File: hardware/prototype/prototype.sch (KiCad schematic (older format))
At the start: 17 parts

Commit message: semi-finaliseprototype gateway design
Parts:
- removed J?: Jack-DC, symbol Connector_Specialized:Jack-DC
- removed JP? (x6): SolderJumper_3_Open, symbol Jumper:SolderJumper_3_Open
- removed JP? (x3): SolderJumper_2_Open, symbol Jumper:SolderJumper_2_Open
- removed JP? (x2): SolderJumper_2_Bridged, symbol Jumper:SolderJumper_2_Bridged
- added C?: 10uF, symbol Device:C
- added C? (x4): 0.1uF, symbol Device:C
- added J?: Screw_Terminal_01x02, symbol Connector_Specialized:Screw_Terminal_01x02
- added J?: Conn_02x12_Odd_Even, symbol Connector_Generic:Conn_02x12_Odd_Even
- added J?: Battery-holder, symbol battery-holder:Battery-holder
- added J?: Conn_01x03, symbol Connector_Generic:Conn_01x03
- added J?: Conn_01x04, symbol Connector_Generic:Conn_01x04
- added JP? (x26): Jumper_NC_Dual, symbol Device:Jumper_NC_Dual
- added JP? (x2): Jumper_NC_Small, symbol Device:Jumper_NC_Small
- added JP? (x2): SolderJumper_2_Open, symbol Jumper:SolderJumper_2_Open
- added JP? (x3): Jumper_NO_Small, symbol Device:Jumper_NO_Small
- added R?: 10k, symbol Device:R
- added U?: LM2596_MODULE, symbol narra:LM2596_MODULE
- added U?: TLV71333PDBV, Package_TO_SOT_SMD:SOT-23-5, symbol Regulator_Linear:TLV71333PDBV
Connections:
- net labels added: (+)RAIL, (-)RAIL, 1, 10, 12, 14, 15, 16, 17, 18, 19, 2, 21, 22, 23, 24, 3V3_REF, 4, 5, 6, 7, 8, 9, CELLULAR_5V, CONTROLLER_RX, CONTROLLER_TX, CSN, GLOBAL_3V3, GLOBAL_5V, LoRa_5V, MISO, MOSI, PPS, RESET, SCK, TEMP_DATA, TEMP_SCK, V_BCKUP
- net labels removed: 5V, BRD_GPS_RST, HDR_GPS_RST
- wire segments 48 -> 192
- no-connect marks 13 -> 35
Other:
- note added: "3v power_management"
- note added: "5v Input voltage tie-point"
- note added: "5v power_management"
- note added: "Alternate_GPS"
- note added: "Alternative programming header"
- note added: "BAT-HLD-001-xx-OTL CR2032 battery holder"
- note added: "Backup current consumption 7uA @ 3v3(Quectel), 15uA Ublox"
- note added: "Backup supply selection for Cold or Warm/hotstart"
- note added: "Communication_module_header"
- note added: "DHT22 Temp, Humidity sensor\n(vertical)"
- note added: "LoRa concentrator connector(Top view), RF connector on left"
- note added: "On board GPS"
- note added: "RAK_concentrator"
- note added: "RHF0M301_concentrator"
- note added: "TODO\n1. Add reverse polarity protection.\n2. Add ESP32 connections\n3. Check the LAN/Cellular connection compatibility and complete communication header.\n4. Check 3D model availability and clashes\n5. Note items needed from digikey/mouser"
- note added: "UBLOX_GPS_header"
- note removed: "Alternative_GPS_header"
- note removed: "Kaiote standard LoRa concentrator connector"
- note removed: "Power_management"
- moved on the sheet: U?

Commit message: Add missing footprints
1. Think about lightning protection and use of GDTs and TVSs
2. Combine the various board and peripheral libraries into a single unified component.
3. The component should have mounting holes suitable for standoffs and cable ties.
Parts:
- removed C?: 0.1uF, symbol Device:C
- removed JP? (x2): Jumper_NC_Small, symbol Device:Jumper_NC_Small
- added C?: 1uF, symbol Device:C
- added C? (x3): 0.1uF, symbol Device:C
- added C? (x2): 10uF, symbol Device:CP
- added D?: LED, symbol Device:LED
- added MK? (x14): Mounting_Hole, symbol Mechanical:Mounting_Hole
- added Q?: DTC143Z, symbol Transistor_BJT:DTC143Z
- added Q?: Si2323, TO_SOT_Packages_SMD:SOT-23, symbol Si2323CDS:Si2323
- added R?: 200, symbol Device:R
- added TP?: Test_Point_Probe, symbol Connector_Specialized:Test_Point_Probe
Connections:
- net labels added: PPS_OUTPUT
- wire segments 192 -> 217
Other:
- note added: "3v3 power_management"
- note added: "Mounting hole for standoffs for GPS module"
- note added: "Mounting hole for standoffs for communication module"
- note added: "PCB mounting hole for controller module cable ties"
- note added: "PCB mounting holes for SMA connectors"
- note added: "PCB mounting holes for cellular module cable ties"
- note added: "PPS indicator"
- note removed: "3v power_management"
- note removed: "Communication_module_header"
- moved on the sheet: U?

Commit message: prototype gateway PCB creation checkpoint
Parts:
- removed C?: 10uF, symbol Device:C
- removed C?: 0.1uF, symbol Device:C
- removed J?: Conn_01x03, symbol Connector_Generic:Conn_01x03
- removed JP?: SolderJumper_2_Open, symbol Jumper:SolderJumper_2_Open
- removed JP? (x12): Jumper_NC_Dual, symbol Device:Jumper_NC_Dual
- removed JP? (x3): Jumper_NO_Small, symbol Device:Jumper_NO_Small
- removed MK? (x14): Mounting_Hole, symbol Mechanical:Mounting_Hole
- removed TP?: Test_Point_Probe, symbol Connector_Specialized:Test_Point_Probe
- removed U?: UBX_M8Q_GPS_HEADER, symbol quectel_L80:UBX_M8Q_GPS_HEADER
- added C10: 10uF, symbol Device:CP
- added C2, C9: 0.1uF, symbol Device:C
- added C3: 10uF, symbol Device:C
- added J1: 0734120114, digikey-footprints:Molex_734120114_UMC_RF_CONN_Vertical, symbol dk_Coaxial-Connectors-RF:0734120114
- added J4: Conn_01x04, symbol Connector_Generic:Conn_01x04
- added J5: Conn_02x07_Odd_Even, Connector_PinSocket_2.54mm:PinSocket_2x07_P2.54mm_Horizontal, symbol Connector_Generic:Conn_02x07_Odd_Even
- added JP17, JP18: Jumper, symbol Device:Jumper
- added JP19: SolderJumper_2_Open, symbol Jumper:SolderJumper_2_Open
- added JP6: Jumper_3_Open, Connector_PinHeader_2.54mm:PinHeader_1x03_P2.54mm_Vertical, symbol Jumper:Jumper_3_Open
- D1: renamed from D?; footprint (none) -> LED_SMD:LED_0805_2012Metric_Pad0.97x1.50mm_HandSolder
- J2: renamed from J?; footprint (none) -> Connector_PinSocket_2.54mm:PinSocket_1x04_P2.54mm_Vertical
- J6: renamed from J?; footprint (none) -> lib_fp:BAT-HLD-001-xx-OTL
- J7: renamed from J?; footprint (none) -> lib_fp:Hybrid_concentrator
- JP10, JP11, JP12, JP13, JP14, JP15, JP16, JP2, JP3, JP4, JP5, JP7, JP8, JP9: renamed from JP?; footprint (none) -> Connector_PinHeader_2.54mm:PinHeader_1x03_P2.54mm_Vertical
- Q1: renamed from Q?; purhase page (none) -> https://www.digikey.com/product-detail/en/on-semiconductor/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
- R1: renamed from R?; Population status (none) -> NC
- U1: renamed from U?; footprint (none) -> lib_fp:QUECTEL_L80-M39
- U4: renamed from U?; footprint (none) -> lib_fp:ESP32_DEVKITC
- gave numbers to parts that had none: 16
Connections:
- net labels added: 11, 20, 3, CLK, PPS_VISUAL, RMII-RX0, RMII_CLK, RMII_CRS_DV, RMII_MDC, RMII_MDIO, RMII_RX1, RMII_TX0, RMII_TX1, RMII_TX_EN
- net labels removed: 1, 10, 12, 18, 2, 24, 4, 7, 8, 9, BRD_GPS_VCC, GSM_CTS, GSM_RI, GSM_RTS, HDR_GPS_1PPS, HDR_GPS_RX, HDR_GPS_TX, HDR_GPS_VBCKUP, HDR_GPS_VCC, PPS, PPS_OUTPUT, TEMP_SCK
- wire segments 217 -> 225
- no-connect marks 35 -> 33
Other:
- note added: "Ethernet PHY connector(Waveshare LAN8720)"
- note added: "GPIO35-39 are input pins w/o internal pullup capability"
- note added: "GPS FIX indicator"
- note added: "Handle strapping pins GPIO 0 and GPIO 2 on boot"
- note added: "LoRa concentrator connector(Top view), SMA RF connector on left"
- note added: "Remove jumper on 5v rail when USB programming \nto avoid circulationg currents between supplies."
- note removed: "Alternate_GPS"
- note removed: "CTS_ENABLE(DISABLED DEFAULT)"
- note removed: "GPS select jumper"
- note removed: "LoRa concentrator connector(Top view), RF connector on left"
- note removed: "Mounting hole for standoffs for GPS module"
- note removed: "Mounting hole for standoffs for communication module"
- note removed: "On board GPS"
- note removed: "PCB mounting hole for controller module cable ties"
- note removed: "PCB mounting holes for SMA connectors"
- note removed: "PCB mounting holes for cellular module cable ties"
- note removed: "PPS indicator"
- note removed: "RI_ENABLE(DISABLED DEFAULT)"
- note removed: "RTS_ENABLE(DISABLED DEFAULT)"
- note removed: "UBLOX_GPS_header"
- moved on the sheet: C1, C6, C8, J7, JP11, JP15, JP7, JP9

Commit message: Complete schematic less mikroe ug95 footprint
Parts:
- removed J3: Screw_Terminal_01x02, symbol Connector_Specialized:Screw_Terminal_01x02
- added C13: 10uF, Capacitor_SMD:C_1206_3216Metric_Pad1.24x1.80mm_HandSolder, symbol Device:CP
- added C14, C15: 0.1uF, Capacitor_SMD:C_0805_2012Metric_Pad1.15x1.50mm_HandSolder, symbol Device:C
- added C16: 220uF, Capacitor_SMD:CP_Elec_6.3x5.8, symbol Device:CP
- added D2: LED, LED_SMD:LED_0805_2012Metric_Pad0.97x1.50mm_HandSolder, symbol Device:LED
- added J8: Jack-DC, Connector_BarrelJack:BarrelJack_Horizontal, symbol Connector_Specialized:Jack-DC
- added JP20: Jumper, Connector_PinSocket_2.54mm:PinSocket_1x02_P2.54mm_Vertical, symbol Device:Jumper
- added R3, R4, R7: 10k, Resistor_SMD:R_0805_2012Metric, symbol Device:R
- added R6: 270R, Resistor_SMD:R_0805_2012Metric, symbol Device:R
- added R8: 33R, Resistor_SMD:R_0805_2012Metric, symbol Device:R
- C1, C12, C2, C5, C8: footprint (none) -> Capacitor_SMD:C_0805_2012Metric_Pad1.15x1.50mm_HandSolder
- C10, C11: value 10uF -> 220uF; footprint (none) -> Capacitor_SMD:CP_Elec_6.3x5.8; purchase page (none) -> https://www.digikey.com/product-detail/en/nichicon/UUD0J221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
- C3: footprint (none) -> Capacitor_SMD:C_0805_2012Metric_Pad1.15x1.50mm_HandSolder; purchase page (none) -> https://www.digikey.com/product-detail/en/avx-corporation/T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
- C4: value 0.1uF -> 1uF; footprint (none) -> Capacitor_SMD:C_0805_2012Metric_Pad1.15x1.50mm_HandSolder; purchase page (none) -> https://www.digikey.com/product-detail/en/yageo/CC0805KKX7R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
- C6: footprint (none) -> Capacitor_SMD:C_1206_3216Metric_Pad1.24x1.80mm_HandSolder
- C7: value 1uF -> 0.1uF; footprint (none) -> Capacitor_SMD:C_0805_2012Metric_Pad1.15x1.50mm_HandSolder
- C9: value 0.1uF -> 100pF; footprint (none) -> Capacitor_SMD:C_0805_2012Metric_Pad1.15x1.50mm_HandSolder; purchase page (none) -> https://www.digikey.com/product-detail/en/avx-corporation/0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
- J4: footprint (none) -> Connector_PinHeader_2.54mm:PinHeader_1x04_P2.54mm_Vertical
- JP1, JP19: footprint (none) -> Jumper:SolderJumper-2_P1.3mm_Open_RoundedPad1.0x1.5mm
- JP17, JP18: footprint (none) -> Connector_PinSocket_2.54mm:PinSocket_1x02_P2.54mm_Vertical
- Q1: footprint (none) -> Package_TO_SOT_SMD:SC-59_Handsoldering; purchase page (none) -> https://www.digikey.com/product-detail/en/rohm-semiconducto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; purhase page https://www.digikey.com/product-detail/en/on-semiconductor/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 -> (none)
- Q2: purchase page (none) -> https://www.digikey.com/product-detail/en/vishay-siliconix/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
- R1, R2: footprint (none) -> Resistor_SMD:R_0805_2012Metric
- TP1: footprint (none) -> TestPoint:TestPoint_Pad_D1.0mm
- U2: purchase page (none) -> https://www.digikey.ca/product-detail/en/texas-instruments/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
- U3: footprint (none) -> lib_fp:LM2596_MODULE; purchase page (none) -> https://store.nerokas.co.ke/index.php?route=product/product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
- U4: purchase page (none) -> https://www.digikey.com/product-detail/en/espressif-systems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
- U5: purchase page (none) -> https://www.mikroe.com/3g-ea-click
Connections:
- net labels added: ESP32_5v, NETWORK_STATUS, PHY_POWER_EN, RMII_REFOSC_nINT
- net labels removed: (-)RAIL, 3V3, CLK, RMII_CLK
- wire segments 225 -> 271
- no-connect marks 33 -> 39
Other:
- note added: "1PPS output to LED/ uFL connector"
- note added: "Backup supply selection for SRAM in Cold or Warm/hotstart"
- note added: "Handle strapping pins GPIO 0, 2, 5, 12, 15 on boot\n(Set as outputs or handle their state on reset if inputs)"
- note added: "In RHF0M301 Datasheet p20, filtering \ncircuit on RESET line is ignored as \nthere are no mechanical components \non that line."
- note added: "LoRa concentrator connector(Top view), SMA RF connector on right"
- note added: "Network status LED\n=================\nToggles once every 500ms for a network error. Check network interfaces.\nToggles once every 30 sec for a successful uplink report."
- note added: "RMII_REFOSC_nINT should be a 33 ohm transmission line"
- note added: "Remove jumper on 5v rail when USB programming \nto avoid circulating currents between supplies."
- note removed: "Backup supply selection for Cold or Warm/hotstart"
- note removed: "Handle strapping pins GPIO 0 and GPIO 2 on boot"
- note removed: "LoRa concentrator connector(Top view), SMA RF connector on left"
- note removed: "Remove jumper on 5v rail when USB programming \nto avoid circulationg currents between supplies."
- note removed: "TODO\n1. Add reverse polarity protection.\n2. Add ESP32 connections\n3. Check the LAN/Cellular connection compatibility and complete communication header.\n4. Check 3D model availability and clashes\n5. Note items needed from digikey/mouser"
- moved on the sheet: C1, C10, C4, C8, J7, JP11, JP17

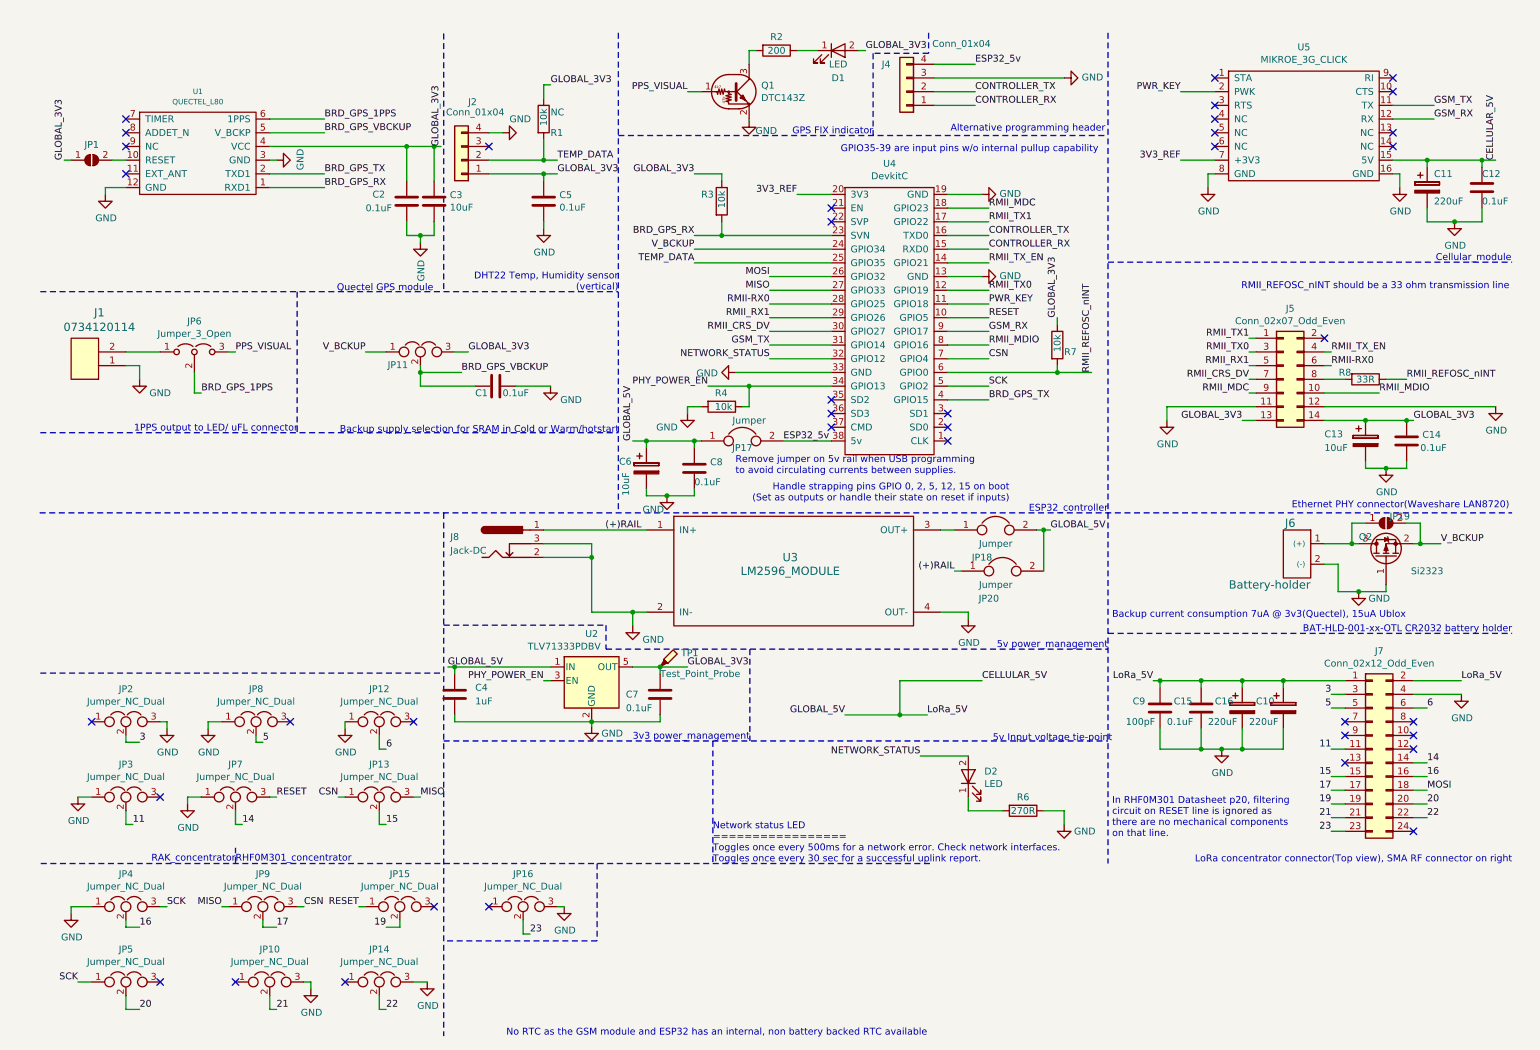
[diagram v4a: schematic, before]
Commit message: Complete schematic design less footprint asignment completion
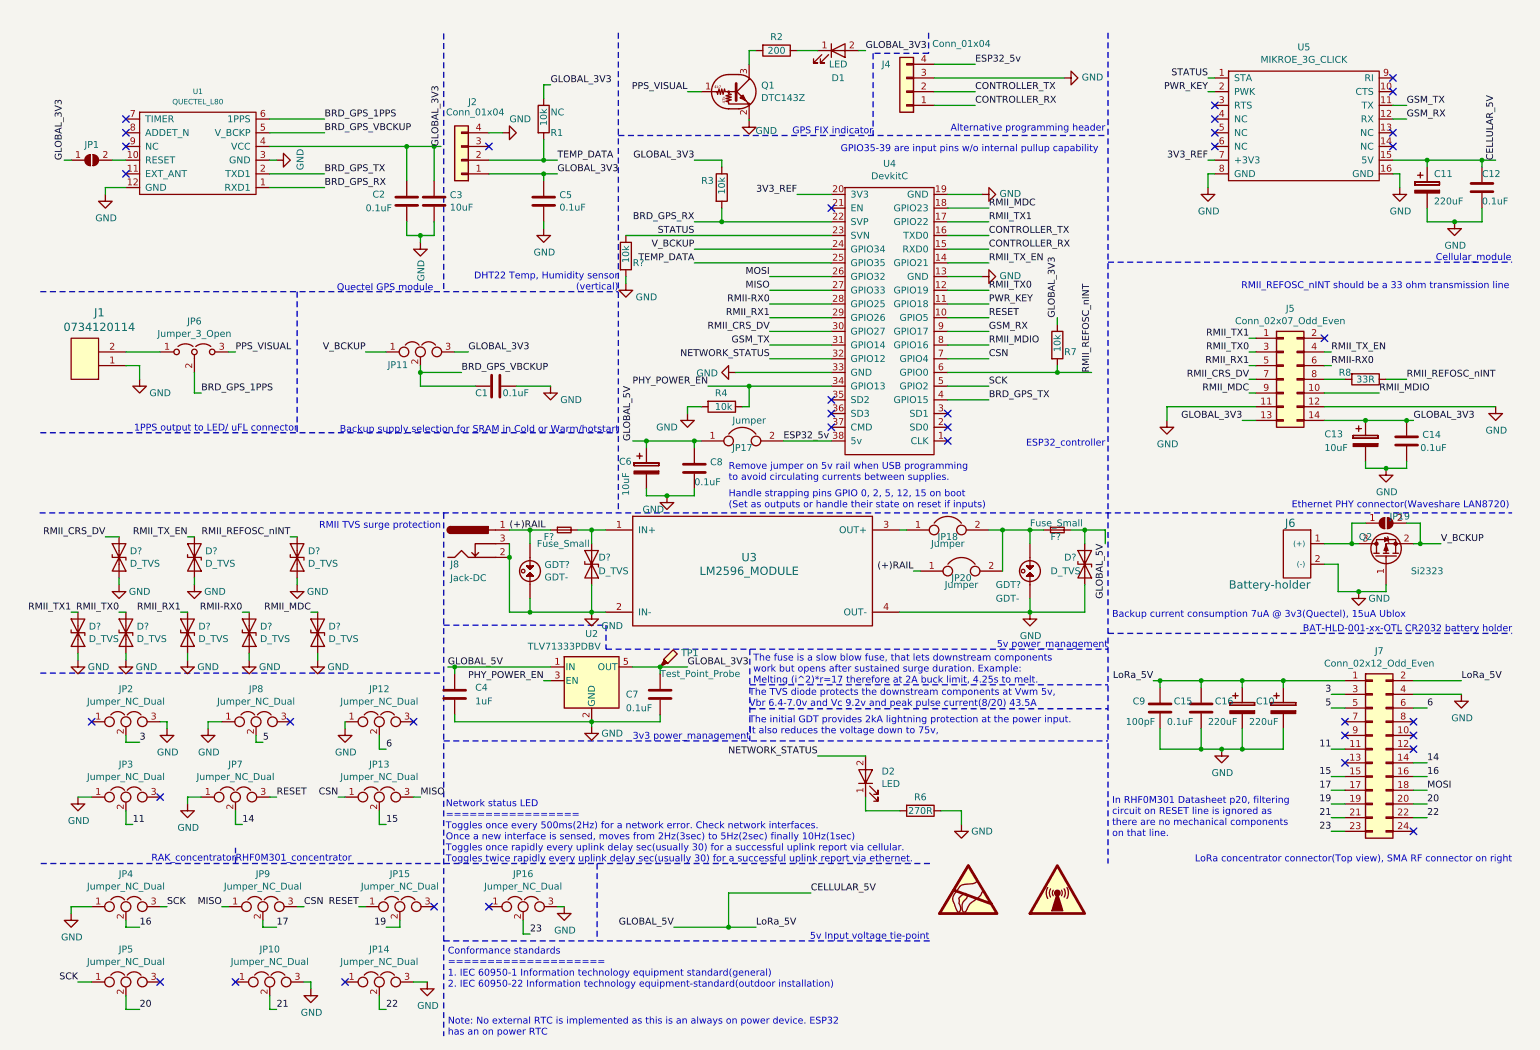
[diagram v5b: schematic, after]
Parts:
- added D? (x10): D_TVS, symbol Device:D_TVS
- added F? (x2): Fuse_Small, symbol Device:Fuse_Small
- added GDT? (x2): GDT-, symbol GDT-:GDT-
- added R?: 10k, symbol Device:R
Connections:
- net (+)RAIL: now also F?.1, GDT?.1; no longer U3.1 (IN+)
- net BRD_GPS_RX: now also U4.22 (SVP); no longer U4.23 (SVN)
- net CELLULAR_5V: now also D?.1 (A1), F?.2; no longer JP18.2, JP20.2
- net GND: now also D?.2 (A2), D?.2 (A2), D?.2 (A2), D?.2 (A2), D?.2 (A2), D?.2 (A2), D?.2 (A2), D?.2 (A2), D?.2 (A2), D?.2 (A2), GDT?.2, GDT?.2, R?.2
- net RMII-RX0: now also D?.1 (A1)
- net RMII_CRS_DV: now also D?.1 (A1)
- net RMII_MDC: now also D?.1 (A1)
- net RMII_REFOSC_nINT: now also D?.1 (A1)
- net RMII_RX1: now also D?.1 (A1)
- net RMII_TX0: now also D?.1 (A1)
- net RMII_TX1: now also D?.1 (A1)
- net RMII_TX_EN: now also D?.1 (A1)
- net STATUS: now reaches U5.1 (STA)
- net STATUS: now also U4.23 (SVN), R?.1
- new net: D?.1 (A1), F?.2, U3.1 (IN+)
- new net: F?.1, GDT?.1, JP18.2, JP20.2
- no-connect marks 39 -> 37
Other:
- note added: "Conformance standards\n====================\n1. IEC 60950-1 Information technology equipment standard(general)\n2. IEC 60950-22 Information technology equipment-standard(outdoor installation)"
- note added: "Network status LED\n=================\nToggles once every 500ms(2Hz) for a network error. Check network interfaces.\nOnce a new interface is sensed, moves from 2Hz(3sec) to 5Hz(2sec) finally 10Hz(1sec)\nToggles once rapidly every uplink delay sec(usually 30) for a successful uplink report via cellular.\nToggles twice rapidly every uplink delay sec(usually 30) for a successful uplink report via et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"
- note added: "Note: No external RTC is implemented as this is an always on power device. ESP32 \nhas an on power RTC"
- note added: "RMII TVS surge protection"
- note added: "The TVS diode protects the downstream components at Vwm 5v, \nVbr 6.4-7.0v and Vc 9.2v and peak pulse current(8/20) 43.5A"
- note added: "The fuse is a slow blow fuse, that lets downstream components\nwork but opens after sustained surge duration. Example:\nMelting (i^2)*r=17 therefore at 2A buck limit, 4.25s to melt."
- note added: "The initial GDT provides 2kA lightning protection at the power input.\nIt also reduces the voltage down to 75v,"
- note removed: "Network status LED\n=================\nToggles once every 500ms for a network error. Check network interfaces.\nToggles once every 30 sec for a successful uplink report."
- note removed: "No RTC as the GSM module and ESP32 has an internal, non battery backed RTC available"
- moved on the sheet: D2, J8, JP18, JP20, R3, R6, U3
